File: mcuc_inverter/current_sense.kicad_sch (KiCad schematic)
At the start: 0 parts

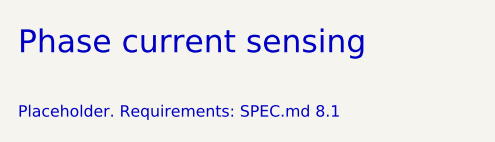
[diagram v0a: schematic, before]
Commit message: Design the supervisor interlock block
Adds docs/supervisor.md: the full logic design for the firmware-independent
hardware interlocks required by SPEC.md §9.2 -- overcurrent detect and latch,
fault aggregation, PWM overlap elimination and dead time. Includes the
24-signal interface, gate budget, and a failure-mode review done on the
assumption that firmware is hostile.

Two selections differ from the original PALTA board, both deliberate:

- Comparators run from +5 V, not 3.3 V. The LM2903's input common-mode
  ceiling is VCC-1.5V, so on 3.3 V it is 1.8 V -- below the 3.05 V positive
  trip point. The positive-overcurrent channel would never have asserted.
  Open-drain outputs still pull up to 3.3 V, so no level shifting is needed.
- 74HC replaces 74ACT. The dead-time RC assumes a CMOS threshold at
  0.5*VCC; 74ACT's TTL thresholds make the delay supply- and part-dependent.
  Predictable dead time beats ~10 ns of propagation delay here.

Adds tools/gen_skeleton.py, which generates the KiCad skeleton and records
the block interfaces, and ERC severities in mcuc_inverter.kicad_pro:
hier_label_mismatch stays an error, label_dangling and pin_not_connected
become warnings during build-out.

The interface is not emitted into the schematic yet (EMIT_INTERFACE=False).
Emitting it into empty sheets produces 96 legitimate dangling-label
violations, and copperhead check fails on warnings as well as errors, which
would leave the verification gate permanently red -- the same failure mode
that let the earlier generated documents through unchecked. The interface
lands in the same change as the components. Rationale in supervisor.md §9.

Verified: kicad-cli sch erc reports 0 violations and copperhead check is
green. With the interface temporarily emitted, ERC reported no
hier_label_mismatch, confirming all 24 names and directions agree across
every sheet boundary.

Co-Authored-By: Claude Opus 5 <noreply@anthropic.com>
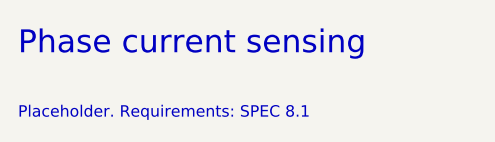
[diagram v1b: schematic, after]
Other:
- note added: "Placeholder. Requirements: SPEC 8.1"
- note removed: "Placeholder. Requirements: SPEC.md 8.1"
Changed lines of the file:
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@@
 		)
 	)
-	(text "Placeholder. Requirements: SPEC.md 8.1"
+	(text "Placeholder. Requirements: SPEC 8.1"
 		(exclude_from_sim no)
 		(at 20 27 0)

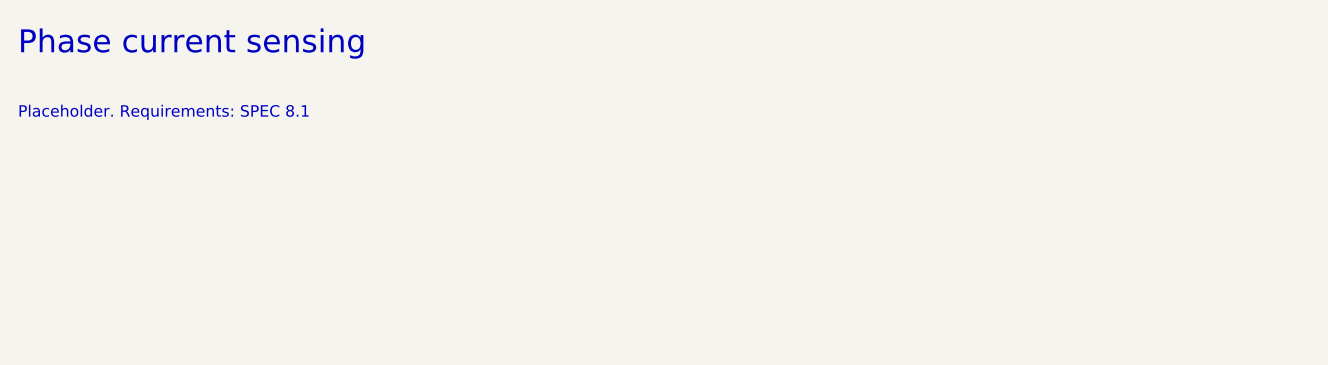
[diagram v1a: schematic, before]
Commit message: Place the supervisor overcurrent comparator front end
Implements docs/supervisor.md section 3 in the schematic: 13 components
across the threshold divider, six LM2903 comparator channels and the
wired-OR trip node.

A single three-resistor string (1k / 11k / 1k off +3V3) generates both
thresholds -- 3.046 V and 0.254 V, i.e. +/-280 A -- which keeps them
ratiometric with the rail the current sense is referenced to, so divider
tolerance and rail drift track out of the trip point.

Channel polarity: the positive trip puts V_TH_POS on IN+ and ISENSE on
IN-, the negative trip the other way round, so both pull the open-drain
output low on an overcurrent of either sign. All six outputs wire-OR onto
OC_TRIP_N with one 4.7k pull-up to +3V3 and a 100 pF filter.

Verified by netlist export rather than assumption:
  OC_TRIP_N  8 nodes  six comparator outputs + pull-up + filter
  V_TH_POS   6 nodes  divider tap, decoupling, three positive-channel IN+
  V_TH_NEG   6 nodes  divider tap, decoupling, three negative-channel IN-
  ISENSE_x   2 nodes  Ux.2 and Ux.5, the intended cross-pairing
  +5V        6 nodes  three LM2903 V+ and three decoupling caps
  GND       10 nodes
ERC reports 0 errors.

gen_skeleton.py now emits interface signals selectively via EMIT_SIGNALS
instead of all-or-nothing, so warnings stay proportional to what is built.
Six warnings remain -- 3 label_dangling and 3 pin_not_driven -- all saying
that current_sense does not exist yet so nothing drives ISENSE. Left in
place deliberately; they clear when that block is populated.

pin_not_driven joins the WIP warning severities. hier_label_mismatch stays
an error, since a boundary mismatch is a real defect at any build state.

Note that copperhead check fails on warnings as well as errors, so it reads
red while any block is unbuilt. kicad-cli sch erc --severity-error is the
meaningful gate during build-out and currently reports 0.

Co-Authored-By: Claude Opus 5 <noreply@anthropic.com>
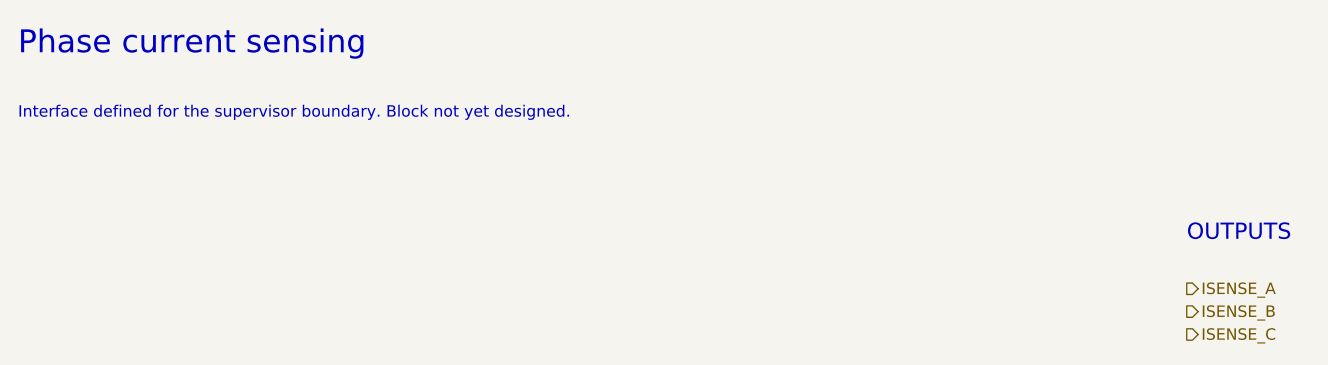
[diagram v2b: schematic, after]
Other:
- note added: "Interface defined for the supervisor boundary. Block not yet designed."
- note added: "OUTPUTS"
- note removed: "Placeholder. Requirements: SPEC 8.1"
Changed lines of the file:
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@@
 		)
 	)
-	(text "Placeholder. Requirements: SPEC 8.1"
+	(text "Interface defined for the supervisor boundary. Block not yet designed."
 		(exclude_from_sim no)
 		(at 20 27 0)
@@
 		)
 	)
+	(text "OUTPUTS"
+		(exclude_from_sim no)
+		(at 149.86 40.64 0)
+		(effects
+			(font
+				(size 1.8 1.8)
+			)
+			(justify left bottom)
+		)
+	)
+	(hierarchical_label "ISENSE_A"
+		(shape output)
+		(at 149.86 45.72 0)
+		(fields_autoplaced yes)
+		(effects
+			(font
+				(size 1.27 1.27)
+			)
+			(justify left)
+		)
+	)
+	(hierarchical_label "ISENSE_B"
+		(shape output)
+		(at 149.86 48.26 0)
+		(fields_autoplaced yes)
+		(effects
+			(font
+				(size 1.27 1.27)
+			)
+			(justify left)
+		)
+	)
+	(hierarchical_label "ISENSE_C"
+		(shape output)
+		(at 149.86 50.8 0)
+		(fields_autoplaced yes)
+		(effects
+			(font
+				(size 1.27 1.27)
+			)
+			(justify left)
+		)
+	)
